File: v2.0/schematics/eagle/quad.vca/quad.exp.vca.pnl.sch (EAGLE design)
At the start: 66 parts, among them IC1 TL084P, IC2 LM13700N, IC3 LM13700N, Q1 2N3904, Q2 2N3906, Q3 2N3904, Q4 2N3906, Q5 2N3904, Q6 2N3906, Q7 2N3904, Q8 2N3906

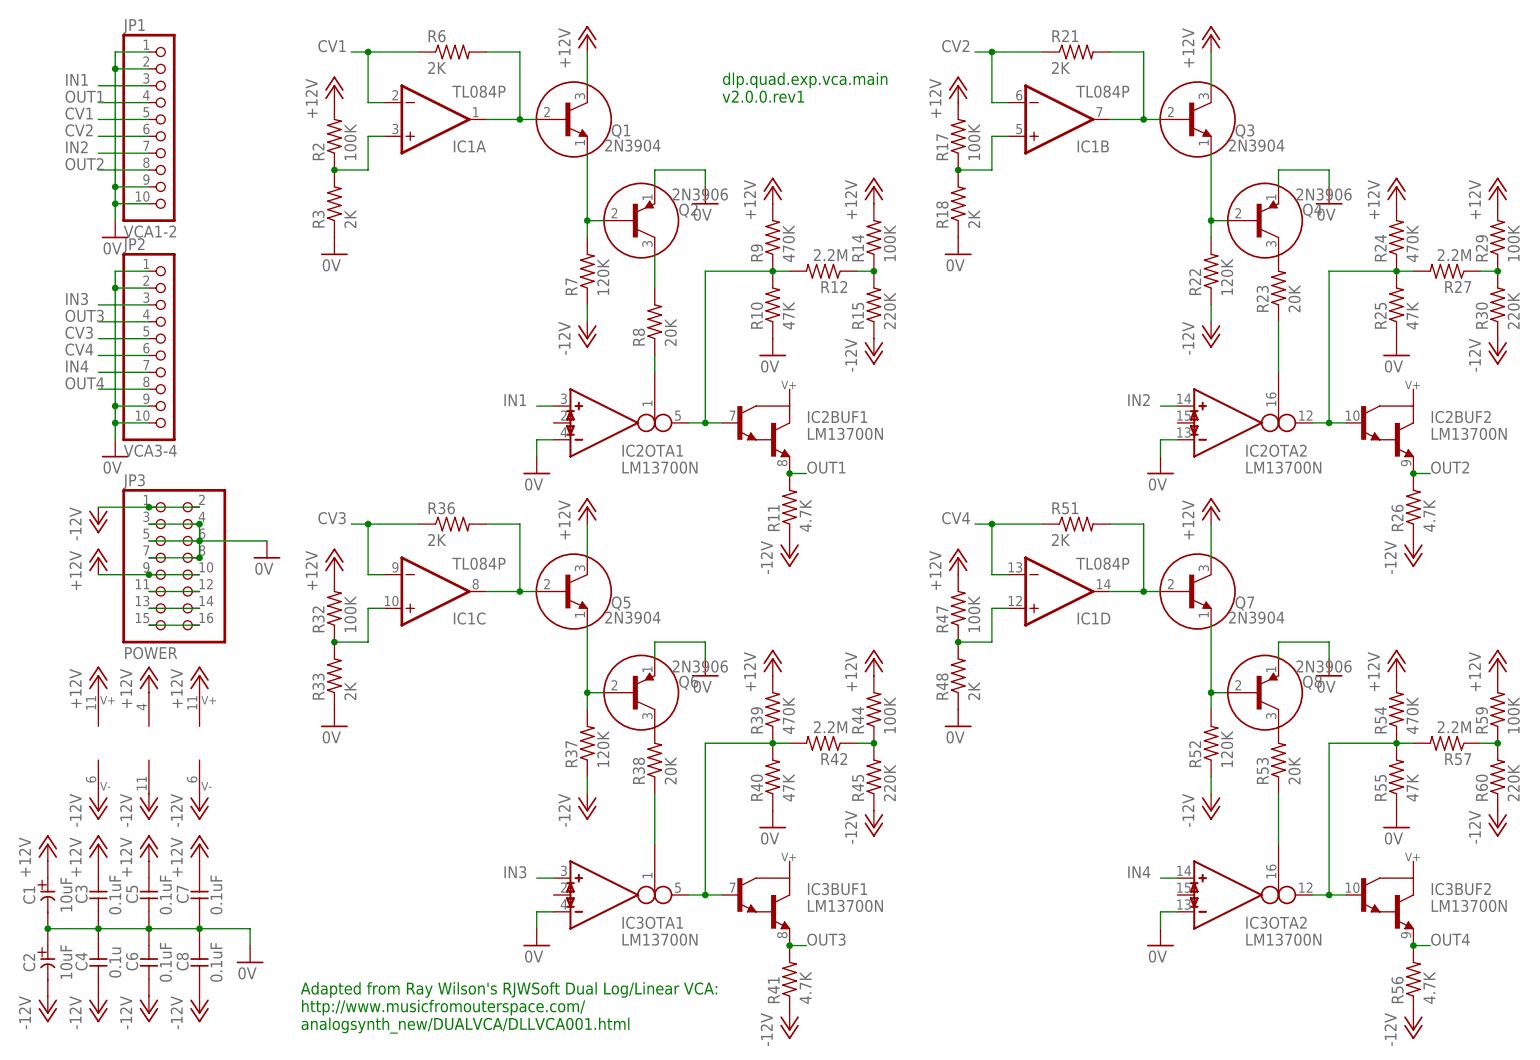
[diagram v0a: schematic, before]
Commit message: Split quad.exp.vca into main and pnl boards with completed autorouting
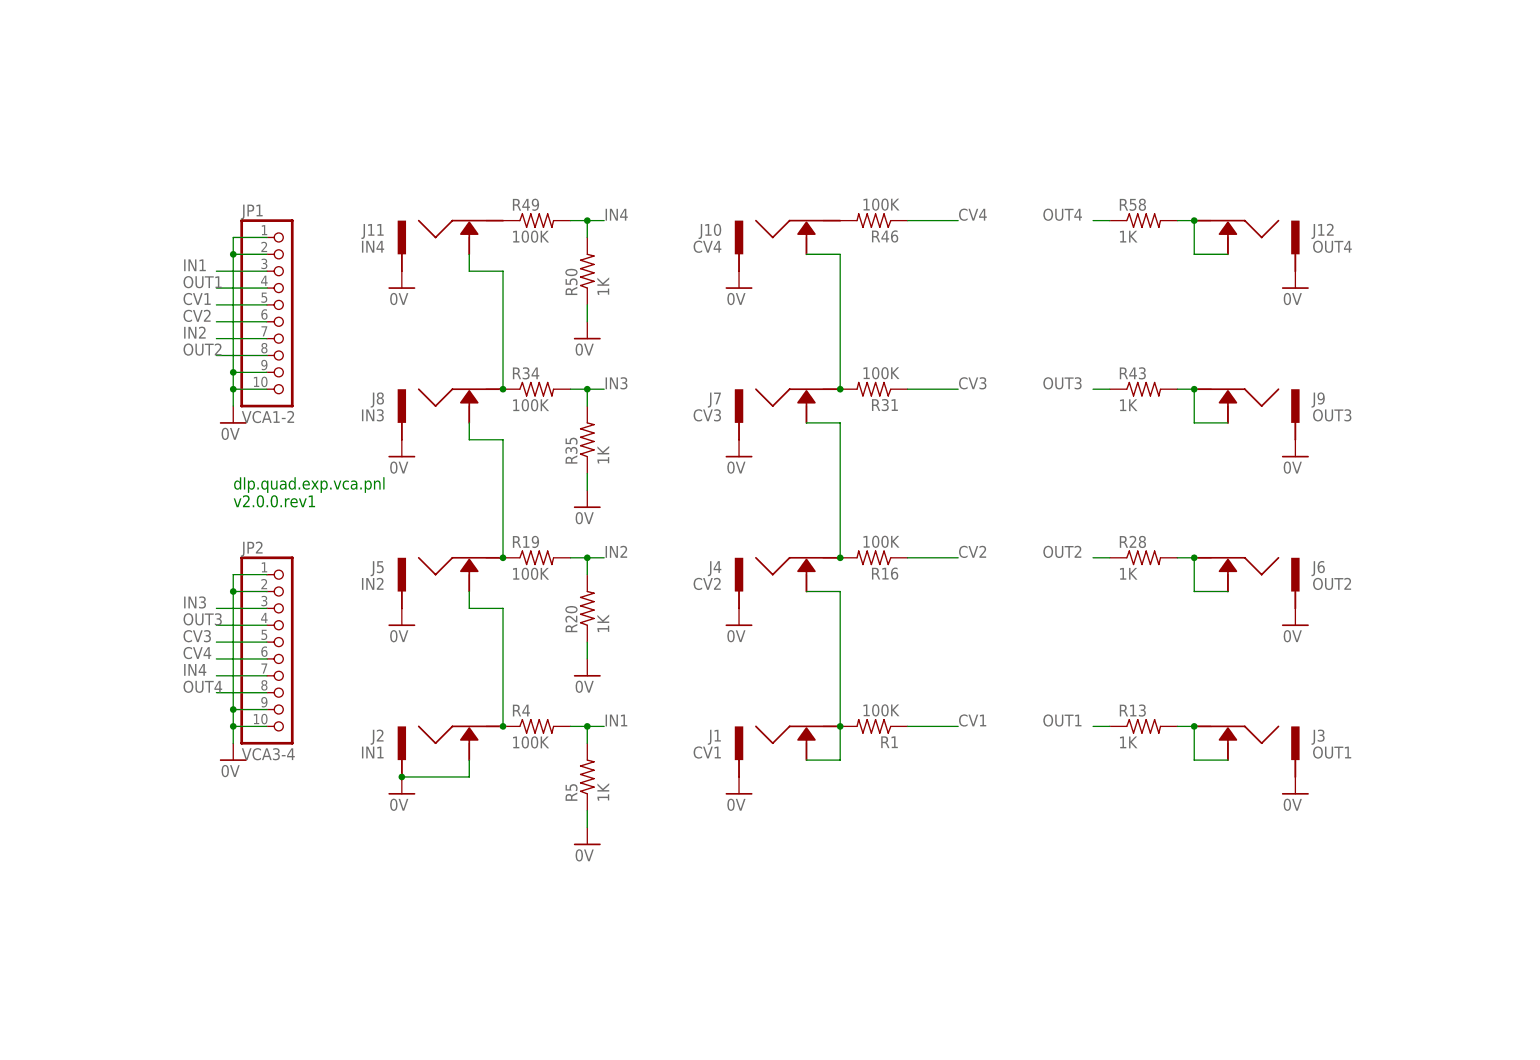
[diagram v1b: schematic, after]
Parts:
- removed C1, C2: 10uF, _common:CE-USE2-5
- removed C3, C5, C6, C7, C8: 0.1uF, _common:CC-US025-024X044
- removed C4: 0.1u, _common:CC-US025-024X044
- removed IC1: TL084P, linear:TL084P
- removed IC2, IC3: LM13700N, ota:LM13700N
- removed JP3: POWER, pinhead:PINHD-2X8
- removed Q1, Q3, Q5, Q7: 2N3904, _common:2N3904
- removed Q2, Q4, Q6, Q8: 2N3906, _common:2N3906
- removed R10, R25, R40, R55: 47K, resistor:R-US_0207/7
- removed R11, R26, R41, R56: 4.7K, resistor:R-US_0207/7
- removed R12, R27, R42, R57: 2.2M, resistor:R-US_0207/7
- removed R14, R17, R2, R29, R32, R44, R47, R59: 100K, resistor:R-US_0207/7
- removed R15, R30, R45, R60: 220K, resistor:R-US_0207/7
- removed R18, R21, R3, R33, R36, R48, R51, R6: 2K, resistor:R-US_0207/7
- removed R22, R37, R52: 120K, resistor:R-US_0207/7
- removed R23, R38, R53, R8: 20K, resistor:R-US_0207/7
- removed R24, R39, R54, R9: 470K, resistor:R-US_0207/7
- added J1: CV1, jacks:ACJM-MV35-2S
- added J10: CV4, jacks:ACJM-MV35-2S
- added J11: IN4, jacks:ACJM-MV35-2S
- added J12: OUT4, jacks:ACJM-MV35-2S
- added J2: IN1, jacks:ACJM-MV35-2S
- added J3: OUT1, jacks:ACJM-MV35-2S
- added J4: CV2, jacks:ACJM-MV35-2S
- added J5: IN2, jacks:ACJM-MV35-2S
- added J6: OUT2, jacks:ACJM-MV35-2S
- added J7: CV3, jacks:ACJM-MV35-2S
- added J8: IN3, jacks:ACJM-MV35-2S
- added J9: OUT3, jacks:ACJM-MV35-2S
- added R1, R16, R19, R31, R34, R4, R46, R49: 100K, resistor:R-US_0207/7
- added R13, R20, R28, R35, R43, R5, R58: 1K, resistor:R-US_0207/7
- R50: value 120K -> 1K
- renumbered R7 to R50
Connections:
- removed net +12V: C1.+, C3.1, C5.1, C7.1, IC1P.V+, IC2SUPPLY.V+, IC3SUPPLY.V+, JP3.10, JP3.9, Q1.C, Q3.C, Q5.C, Q7.C, R14.2, R17.2, R2.2, R24.2, R29.2, R32.2, R39.2, R44.2, R47.2, R54.2, R59.2, R9.2
- removed net -12V: C2.-, C4.2, C6.2, C8.2, IC1P.V-, IC2SUPPLY.V-, IC3SUPPLY.V-, JP3.1, JP3.2, R11.1, R15.1, R22.1, R26.1, R30.1, R37.1, R41.1, R45.1, R50.1, R52.1, R56.1, R60.1
- removed net N$10: IC1C.OUT, Q5.B, R36.2
- removed net N$14: Q5.E, Q6.B, R37.2
- removed net N$15: IC2BUF1.B, IC2OTA1.OUT, R10.2, R12.2, R9.1
- removed net N$17: Q4.C, R23.2
- removed net N$20: IC3BUF1.B, IC3OTA1.OUT, R39.1, R40.2, R42.2
- removed net N$21: IC2OTA1.I_BIAS, R8.1
- removed net N$25: IC1B.+IN, R17.1, R18.2
- removed net N$27: IC3OTA1.I_BIAS, R38.1
- removed net N$28: IC1B.OUT, Q3.B, R21.2
- removed net N$29: Q3.E, Q4.B, R22.2
- removed net N$30: Q8.C, R53.2
- removed net N$34: IC1D.+IN, R47.1, R48.2
- removed net N$35: IC2BUF2.B, IC2OTA2.OUT, R24.1, R25.2, R27.2
- removed net N$39: IC1D.OUT, Q7.B, R51.2
- removed net N$40: Q7.E, Q8.B, R52.2
- removed net N$41: Q6.C, R38.2
- removed net N$44: IC2OTA2.I_BIAS, R23.1
- removed net N$45: IC3BUF2.B, IC3OTA2.OUT, R54.1, R55.2, R57.2
- removed net N$48: IC3OTA2.I_BIAS, R53.1
- removed net N$49: R12.1, R14.1, R15.2
- removed net N$50: R27.1, R29.1, R30.2
- removed net N$51: R42.1, R44.1, R45.2
- removed net N$52: R57.1, R59.1, R60.2
- removed net N$55: JP3.11, JP3.12
- removed net N$56: JP3.13, JP3.14
- removed net N$57: JP3.15, JP3.16
- removed net N$9: Q2.C, R8.2
- new net N$1: J9.P$2, J9.P$3, R43.2
- new net N$16: J1.P$2, J1.P$3, J4.P$3, R1.2
- new net N$2: J3.P$2, J3.P$3, R13.2
- new net N$24: J6.P$2, J6.P$3, R28.2
- new net N$31: J12.P$2, J12.P$3, R58.2
- new net N$4: J5.P$2, J8.P$3, R19.1
- new net N$42: J11.P$2, R49.1
- new net N$8: J4.P$2, J7.P$3, R16.2
- net 0V: now also J1.P$1, J10.P$1, J11.P$1, J12.P$1, J2.P$1, J2.P$3, J3.P$1, J4.P$1, J5.P$1, J6.P$1, J7.P$1, J8.P$1, J9.P$1, R20.1, R35.1, R5.1, R50.1; no longer C1.-, C2.+, C3.2, C4.1, C5.2, C6.1, C7.2, C8.1, IC2OTA1.IN_N, IC2OTA2.IN_N, IC3OTA1.IN_N, IC3OTA2.IN_N, JP3.3, JP3.4, JP3.5, JP3.6, JP3.7, JP3.8, Q2.E, Q4.E, Q6.E, Q8.E, R10.1, R18.1, R25.1, R3.1, R33.1, R40.1, R48.1, R55.1
- net CV1: now also R1.1; no longer IC1A.-IN, R6.1
- net CV2: now also R16.1; no longer IC1B.-IN, R21.1
- net CV3: now also R31.1; no longer IC1C.-IN, R36.1
- net CV4: now also R46.1; no longer IC1D.-IN, R51.1
- net IN1: now also R4.2, R5.2; no longer IC2OTA1.IN_P
- net IN2: now also R19.2, R20.2; no longer IC2OTA2.IN_P
- net IN3: now also R34.2, R35.2; no longer IC3OTA1.IN_P
- net IN4: now also R49.2, R50.2; no longer IC3OTA2.IN_P
- net N$3: now also J2.P$2, J5.P$3, R4.1; no longer IC1A.+IN, R2.1, R3.2
- net N$5: now also J11.P$3, J8.P$2, R34.1; no longer IC1C.+IN, R32.1, R33.2
- net N$6: now also J10.P$2, R46.2; no longer IC1A.OUT, Q1.B, R6.2
- net N$7: now also J10.P$3, J7.P$2, R31.2; no longer Q1.E, Q2.B, R50.2
- net OUT1: now also R13.1; no longer IC2BUF1.E, R11.2
- net OUT2: now also R28.1; no longer IC2BUF2.E, R26.2
- net OUT3: now also R43.1; no longer IC3BUF1.E, R41.2
- net OUT4: now also R58.1; no longer IC3BUF2.E, R56.2
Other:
- note added: "dlp.quad.exp.vca.pnl v2.0.0.rev1"
- note removed: "Adapted from Ray Wilson's RJWSoft Dual Log/Linear VCA: http://www.musicfromouterspace.com/ analogsynth_new/DUALVCA/DLLVCA001.html"
- note removed: "dlp.quad.exp.vca.main v2.0.0.rev1"
- moved on the sheet: JP1, JP2
